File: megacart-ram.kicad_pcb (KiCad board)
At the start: 2 copper layers, 99.1 x 73.6 mm, 29 parts, among them J1 Conn_02x08_Counter_Clockwise, U1 AS6C4008-55PCN, U10 74HCT32, U11 74HCT32, U12 74HCT138, U13 74HCT273, U2 AS6C62256-55PCN, U3 74HCT74, U4 74HCT21, U5 74HCT21, U6 74HCT02, U7 74HCT04, U8 74HCT08, U9 74HCT08

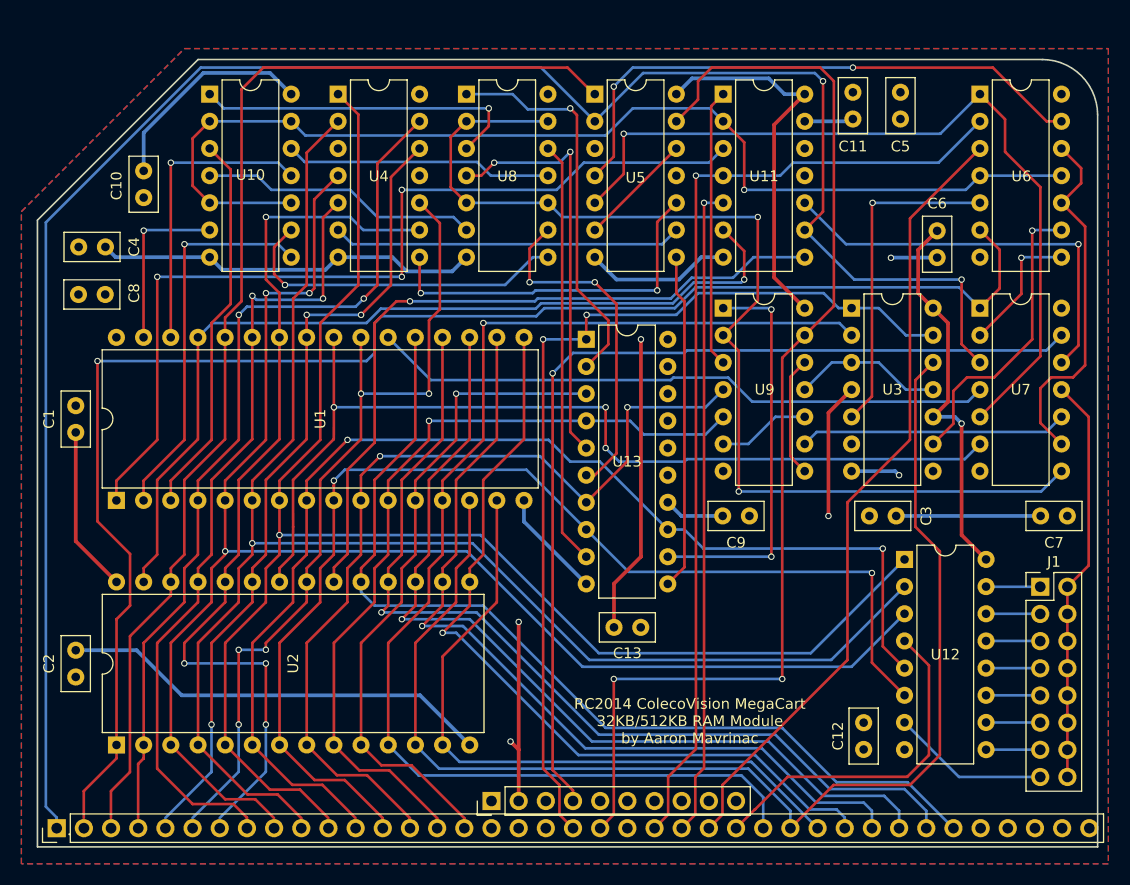
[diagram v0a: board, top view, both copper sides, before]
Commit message: Updated revision of PCB supporting bank mirroring for 64/128/256K MegaCarts.
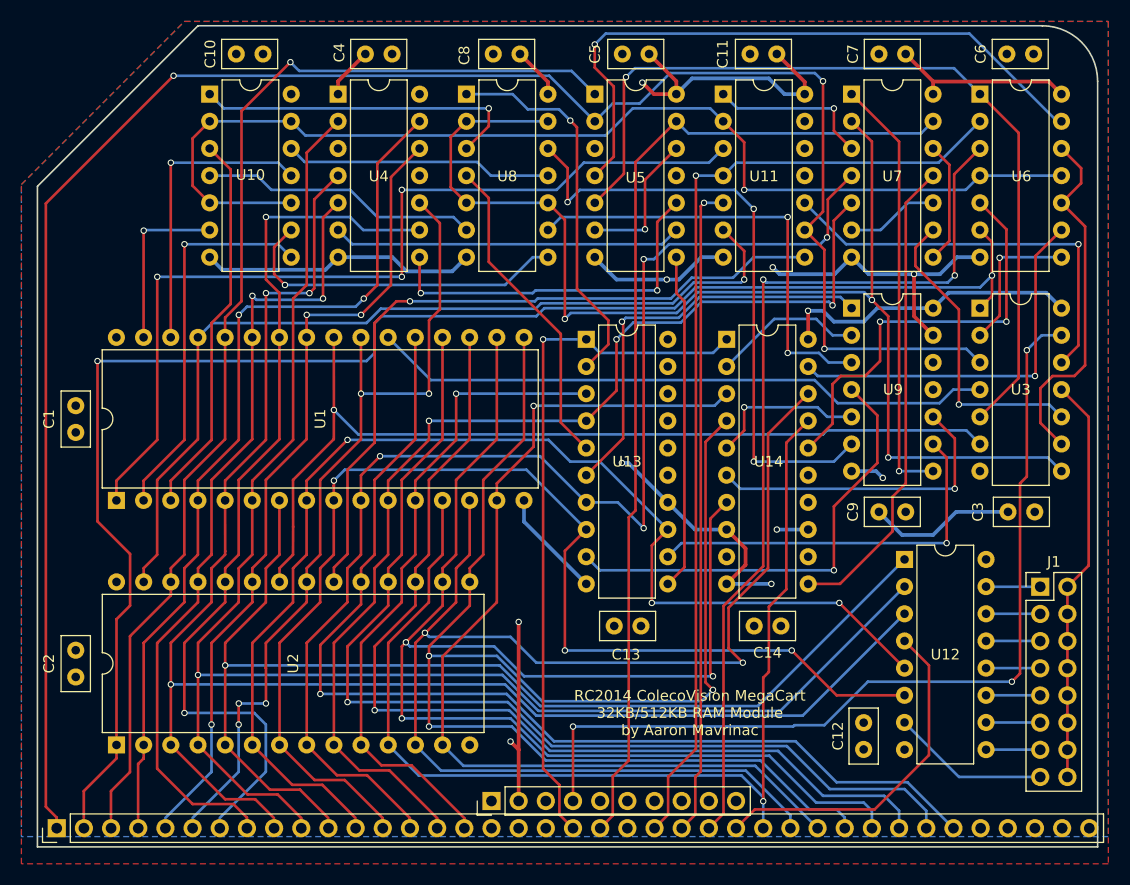
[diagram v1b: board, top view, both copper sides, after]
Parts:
- removed the U3 at (230.0, 103.0)
- added C14: C, Capacitor_THT:C_Disc_D5.0mm_W2.5mm_P2.50mm, F.Cu at (223.4, 132.7)
- added U14: 74HCT273, Package_DIP:DIP-20_W7.62mm, F.Cu at (218.3, 105.9)
- added U7: 74HCT08, Package_DIP:DIP-14_W7.62mm, F.Cu at (230.0, 83.0)
- U9: value 74HCT08 -> 74HCT32
- moved C8 47.0 mm to (199.0, 79.2), turned to 180 degrees
- moved C7 45.7 mm to (235.1, 79.2)
- moved C4 32.3 mm to (184.6, 79.2)
- moved C5 23.8 mm to (211.1, 79.2), turned to 180 degrees
- moved C6 18.8 mm to (247.0, 79.2), turned to 180 degrees
- moved C10 15.6 mm to (175.0, 79.2), turned to 180 degrees
- moved C3 15.5 mm to (247.1, 122.0), turned to 180 degrees
- moved C9 14.6 mm to (235.1, 122.0)
- moved U9 12.0 mm to (230.0, 103.0)
- moved C11 7.96 mm to (223.0, 79.2), turned to 180 degrees
- moved C13 2.52 mm to (210.3, 132.7), turned to 180 degrees
- renumbered U7 to U3
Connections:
- U13 pad 6: Net-(U8-Pad9) -> Net-(U13-Pad6)
- U13 pad 9: Net-(U8-Pad12) -> Net-(U13-Pad9)
- U3 pad 10: Net-(U7-Pad10) -> Net-(U3-Pad10)
- U3 pad 8: Net-(U7-Pad8) -> Net-(U3-Pad8)
- U4 pad 1: A5 -> VCC
- U8 pad 10: Net-(U7-Pad8) -> Net-(U3-Pad8)
- U8 pad 12: Net-(U8-Pad12) -> Net-(U9-Pad6)
- U8 pad 13: Net-(U7-Pad8) -> Net-(U3-Pad8)
- U8 pad 2: Net-(U7-Pad8) -> Net-(U3-Pad8)
- U8 pad 5: Net-(U7-Pad8) -> Net-(U3-Pad8)
- U8 pad 9: Net-(U8-Pad9) -> Net-(U9-Pad3)
- U9 pad 1: Net-(U13-Pad12) -> Net-(U13-Pad6)
- U9 pad 10: Net-(U9-Pad10) -> ~{S4}
- U9 pad 11: Net-(U3-Pad11) -> unconnected-(U9-Pad11)
- U9 pad 12: Net-(U9-Pad12) -> GND
- U9 pad 13: CLK -> GND
- U9 pad 2: Net-(U7-Pad8) -> ~{S2}
- U9 pad 3: Net-(U11-Pad1) -> Net-(U9-Pad3)
- U9 pad 4: A2 -> Net-(U13-Pad9)
- U9 pad 5: A1 -> ~{S3}
- U9 pad 6: Net-(U9-Pad10) -> Net-(U9-Pad6)
- U9 pad 8: Net-(U9-Pad12) -> Net-(U9-Pad8)
- U9 pad 9: Net-(U7-Pad10) -> Net-(U13-Pad12)
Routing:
- net Net-(U3-Pad8): track 0.00 -> 115.2 mm, vias 0 -> 3
- net Net-(U7-Pad8): track 102.8 -> 0.00 mm, vias 2 -> 0
- net VCC: track 166.5 -> 99.8 mm, vias 5 -> 4
- net D3: track 76.5 -> 138.4 mm, vias 1 -> 3
- net Net-(U9-Pad6): track 0.00 -> 57.8 mm, vias 0 -> 3
- net D4: track 80.7 -> 135.4 mm, vias 1 -> 3
- net Net-(U14-Pad11): track 0.00 -> 44.7 mm
- net Net-(U13-Pad9): track 0.00 -> 43.2 mm, vias 0 -> 1
- net Net-(U9-Pad3): track 0.00 -> 42.0 mm, vias 0 -> 2
- net Net-(U9-Pad8): track 0.00 -> 40.3 mm, vias 0 -> 1
- net Net-(U8-Pad12): track 39.6 -> 0.00 mm
- net Net-(U13-Pad6): track 0.00 -> 38.7 mm, vias 0 -> 1
- net A5: track 145.9 -> 108.2 mm
- net A2: track 84.4 -> 120.5 mm, vias 2 -> 4
- net Net-(U8-Pad9): track 32.2 -> 0.00 mm, vias 2 -> 0
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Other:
- board size 99.1 x 73.6 mm -> 99.1 x 76.8 mm

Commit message: Renumber some components.
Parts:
- renumbered C2 to C1, C6 to C12, C3 to C13, C12 to C14, C1 to C2, C13 to C3, C14 to C4, C4 to C5, C5 to C6, U2 to U1, U6 to U12, U3 to U13, U12 to U14, U1 to U2, U13 to U3, U14 to U4, U4 to U5, U5 to U6
